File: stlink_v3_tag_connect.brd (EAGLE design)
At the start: 39.2 x 49.9 mm, 10 parts, among them CON1 STLINK_V3_HAT_SWD/JTAG_MINIMAL, J1 RJ12, U1 SN74LVC2T45DCU

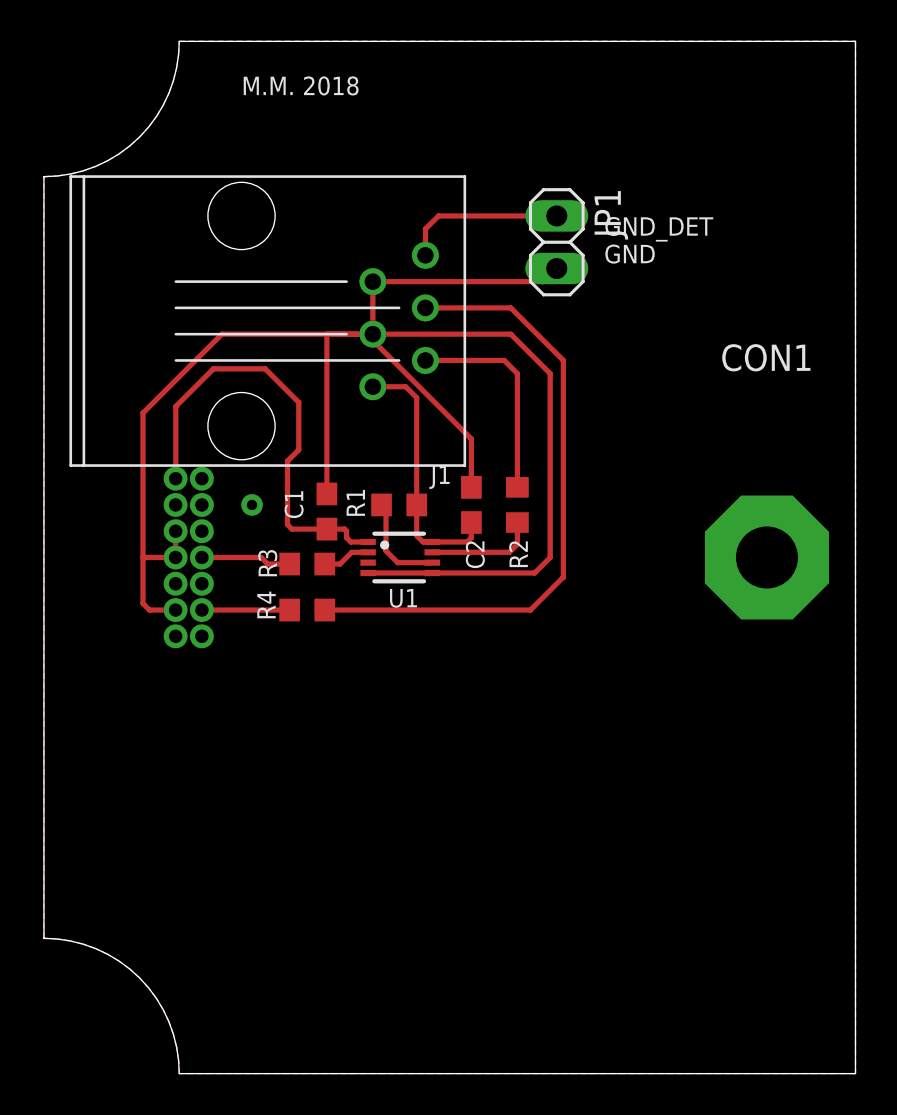
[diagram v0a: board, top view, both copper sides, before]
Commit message: Added SWD popoption
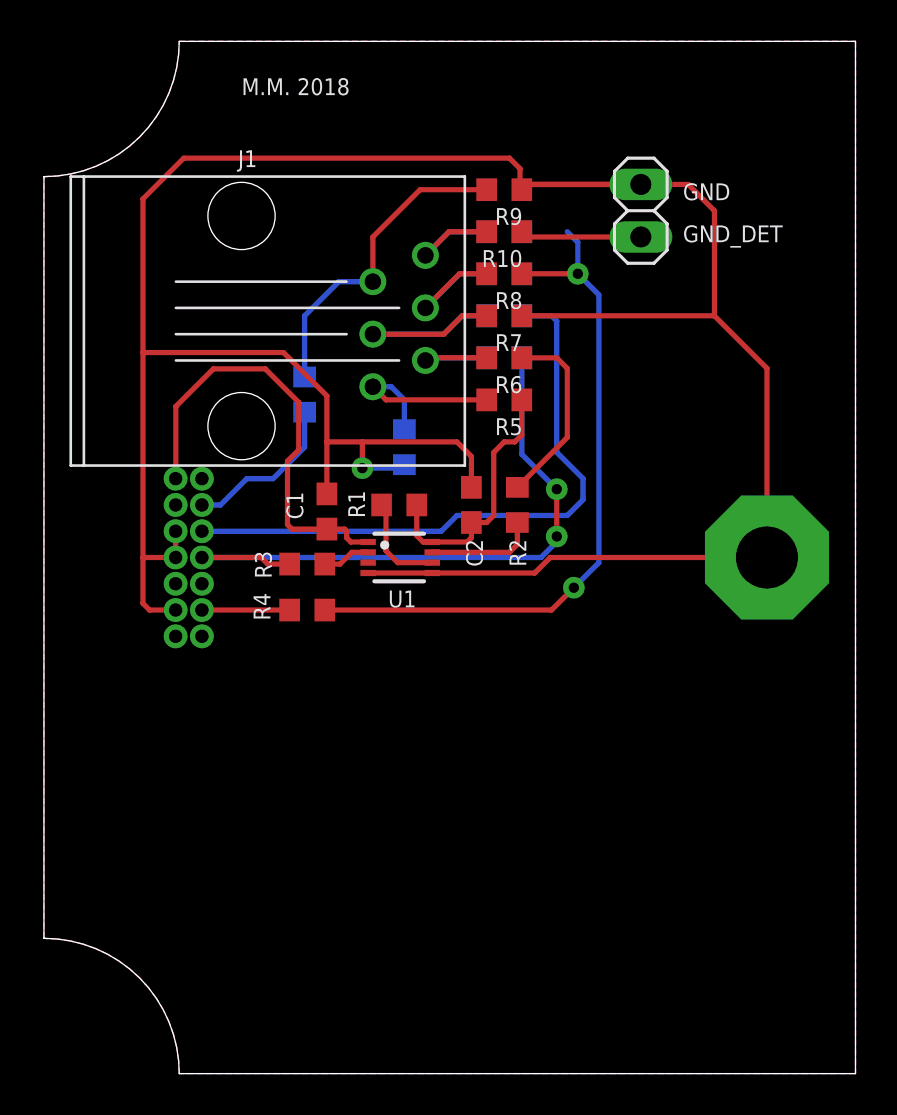
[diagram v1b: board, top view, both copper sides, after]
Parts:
- added R10, R11, R12, R13, R14, R15, R16, R5, R6, R7, R8, R9: 0, resistor:R0603
- JP1: value (none) -> -
- moved JP1 4.34 mm to (-6.10, 16.8), turned to 90 degrees
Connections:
- removed net SWIM_LVL_SHIFTED: CON1.STDC_14_8, R3.1
- removed net SWIM_TARGET: J1.5, R2.2
- removed net VCC_TARGET: C2.1, J1.6, R1.2, U1.8
- new net N$12: J1.6, R11.2, R5.2
- new net N$3: J1.5, R12.2, R6.2
- new net N$4: J1.4, R13.2, R7.2
- new net N$5: J1.3, R14.2, R8.2
- new net N$6: J1.2, R15.2, R9.2
- new net N$7: J1.1, R10.2, R16.2
- new net SWDCLK: CON1.STDC_14_6, R13.1
- new net SWDIO: CON1.STDC_14_4, R15.1
- new net SWIM_DATA: R2.2, R6.1
- new net SWO/SWIM_LVL_SHIFTED: CON1.STDC_14_8, R12.1, R3.1
- net !RESET_TARGET: now also R14.1, R8.1; no longer J1.3
- net DETECT: now also R10.1; no longer J1.1
- net GND: now also R11.1, R7.1, R9.1; no longer J1.2, J1.4
- net SWIM_TARGET_R: now also CON1.STDC_14_10
- net TARGET_VCC: now also C2.1, R1.2, R16.1, R5.1, U1.8
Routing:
- net GND: track 84.8 -> 133.3 mm
- net SWO/SWIM_LVL_SHIFTED: track 0.00 -> 31.4 mm, vias 0 -> 2
- net SWDCLK: track 0.00 -> 30.0 mm
- net N$6: track 0.00 -> 15.6 mm
- net TARGET_VCC: track 0.00 -> 12.7 mm
- net VCC_TARGET: track 12.6 -> 0.00 mm
- net N$4: track 0.00 -> 11.7 mm
- net SWIM_TARGET: track 10.2 -> 0.00 mm
- net SWIM_DATA: track 0.00 -> 9.16 mm
- net N$12: track 0.00 -> 8.99 mm
- net SWDIO: track 0.00 -> 7.81 mm
- net N$5: track 0.00 -> 7.29 mm
- net N$7: track 0.00 -> 6.87 mm
- net N$3: track 0.00 -> 6.03 mm
- net SWIM_LVL_SHIFTED: track 4.37 -> 0.00 mm
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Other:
- board text added: "GND GND_DET"
- board text removed: "GND_DET GND"

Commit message: Routing done
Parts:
- moved R16 7.15 mm to (-19.8, 15.0), turned to 180 degrees
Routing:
- net TARGET_VCC: track 12.7 -> 52.8 mm, vias 0 -> 1
- net SWIM_TARGET_R: track 5.33 -> 42.9 mm, vias 0 -> 2
- net !RESET_TARGET: track 33.5 -> 35.3 mm
- net SWDCLK: track 30.0 -> 31.5 mm
- net SWO/SWIM_LVL_SHIFTED: track 31.4 -> 32.7 mm
- net N$7: track 6.87 -> 6.04 mm
- net SWDIO: track 7.81 -> 8.41 mm

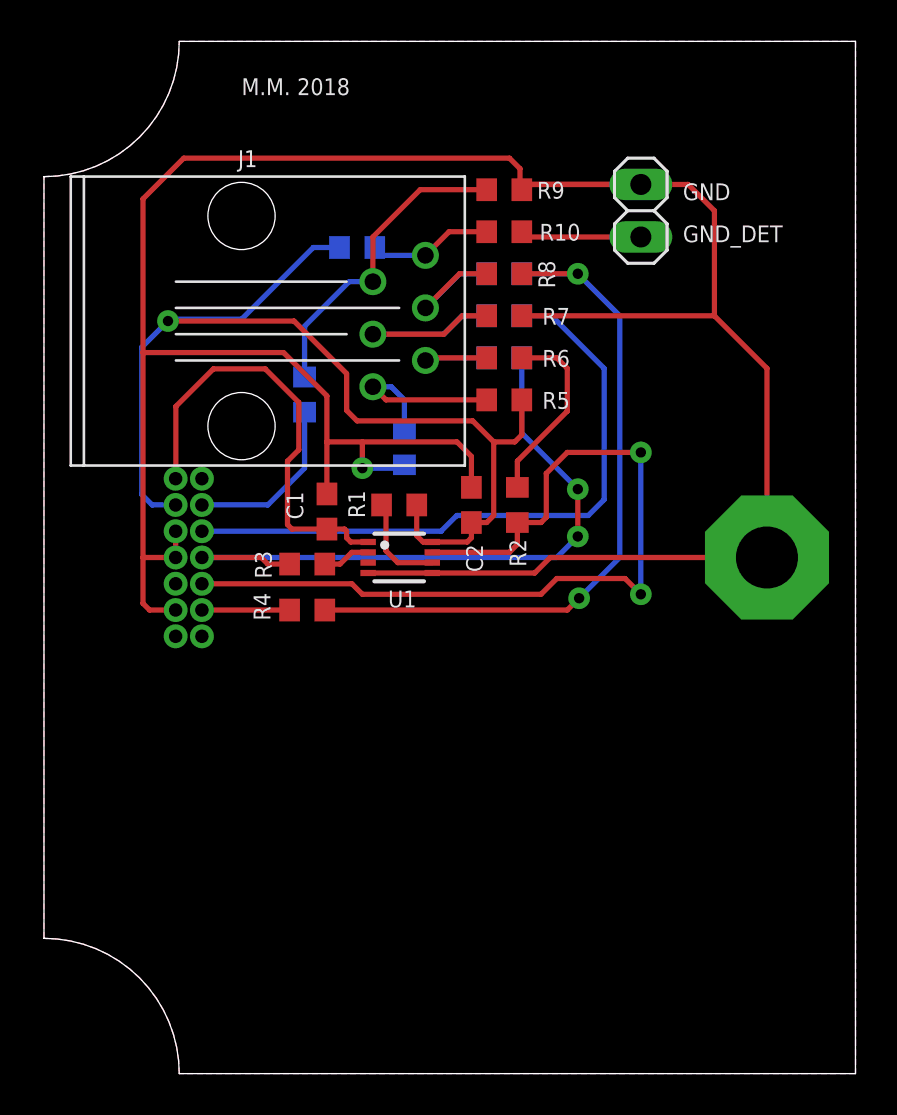
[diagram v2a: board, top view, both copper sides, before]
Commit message: - Added mgt MCU - Moved RJ12 to the middle - Fixed SWD pinout
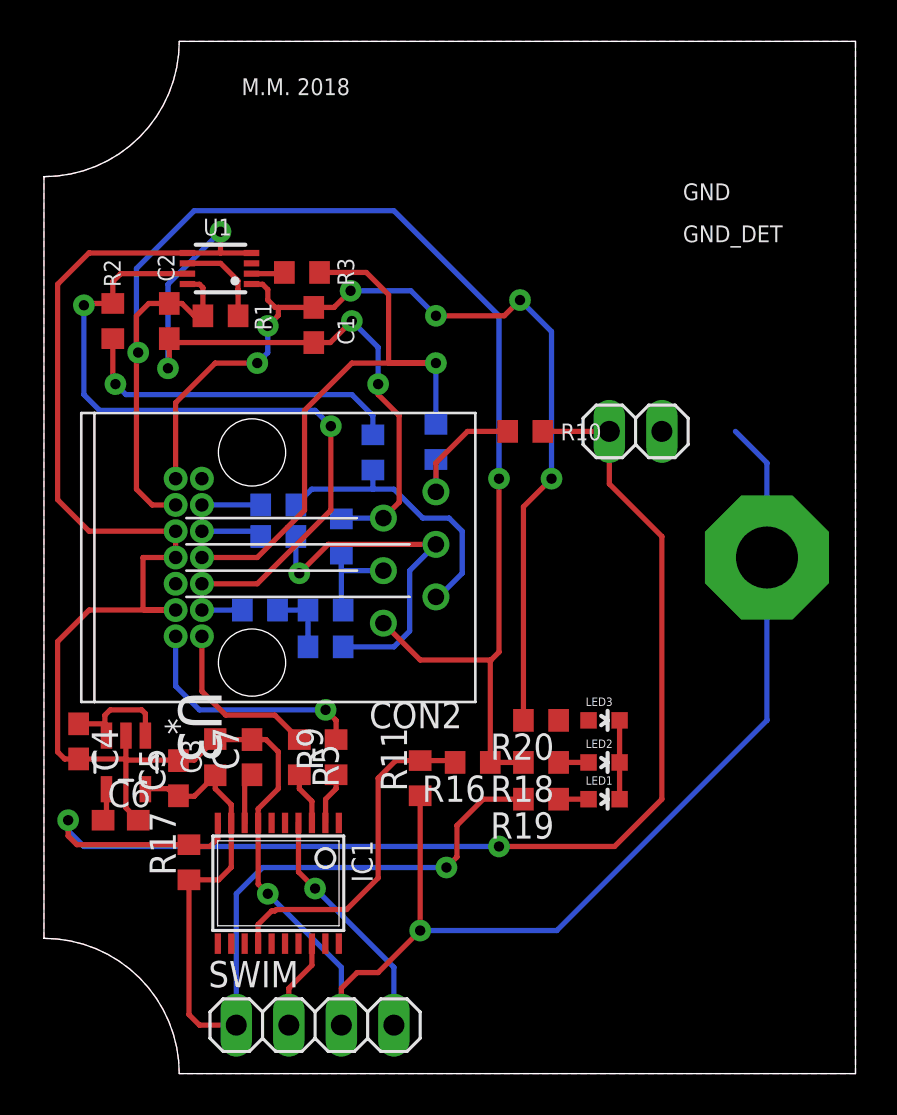
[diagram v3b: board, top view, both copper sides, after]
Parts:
- removed J1: RJ12, con-rj:RJ12
- added C3: 100nF, rcl:C0603K
- added C4, C5, C7: 1uF, rcl:C0603
- added C6: 470pF, rcl:C0603
- added CON2: TC2030-MCP-SWD, tag-connect:RJ12
- added IC1: STM8S003F3, stm8:TSSOP20
- added LED1, LED2, LED3: Red, SparkFun:LED-0603
- added R17: 10K, rcl:R0603
- added R18, R19, R20: 1K, rcl:R0603
- added SWIM: SWIM_254, swim:1X04
- added U3: MIC5205-3.3YM5-TR, LTC_By_element14_Batch_1:SOT95P280X145-5N
- R11, R16: value 0 -> 10K; device resistor:R0603 -> rcl:R0603
- R5, R9: value 0 -> 47; device resistor:R0603 -> rcl:R0603
- moved R9 28.6 mm to (-20.8, -9.65), turned to 90 degrees
- moved R16 25.5 mm to (-14.2, -9.91), flipped to the top
- moved R2 21.5 mm to (-31.6, 11.4), turned to 270 degrees
- moved R8 20.0 mm to (-21.3, -4.32), flipped to the bottom
- moved R5 19.9 mm to (-22.6, -9.65), turned to 270 degrees
- moved R14 18.4 mm to (-21.3, -2.54), turned to 180 degrees
- moved C2 17.1 mm to (-28.9, 11.4), turned to 270 degrees
- moved U1 16.4 mm to (-26.4, 14.0), turned to 90 degrees
- moved R11 16.0 mm to (-16.8, -10.7), flipped to the top
- moved R13 15.3 mm to (-23.6, 1.02), turned to 180 degrees
- moved R3 14.1 mm to (-22.5, 13.8), turned to 180 degrees
- moved R7 13.3 mm to (-20.6, 1.02), flipped to the bottom, turned to 270 degrees
- moved R1 12.6 mm to (-26.4, 11.7), turned to 180 degrees
- moved JP1 10.7 mm to (-6.35, 6.10), turned to 0 degrees
- moved R10 9.71 mm to (-11.7, 6.10)
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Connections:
- removed net N$12: J1.6, R11.2, R5.2
- removed net N$6: J1.2, R15.2, R9.2
- removed net N$7: J1.1, R10.2, R16.2
- new net !RESET_TARGET!/SWDCLK: CON2.3, R13.2, R8.2
- new net !RST: IC1.4, SWIM.4
- new net +3V3: C3.1, C5.1, IC1.9, R17.1, R19.2, SWIM.1, U3.5
- new net DETECT/SWO: CON2.1, R10.2, R12.2
- new net DGND: LED1.C, LED2.C, LED3.C
- new net GND/!RESET_TARGET!: CON2.4, R14.2, R7.2
- new net MIC_BYPASS: C6.1, U3.4
- new net N$2: CON1.STDC_14_14, R5.1
- new net N$38: LED2.A, R18.1
- new net STM8_RX: IC1.3, R5.2
- new net STM8_SWIM: IC1.18, SWIM.2
- new net STM8_TX: IC1.2, R9.1
- new net SWIM_DATA/SWDIO: CON2.5, R15.2, R6.2
- new net TARGET_VCC_DETECT: IC1.14, R11.2, R16.2
- new net VBAT: C4.1, U3.1, U3.3
- new net VCAP1: C7.1, IC1.8
- net DETECT: now also IC1.10, R17.2
- net GND: now also C3.2, C4.2, C5.2, C6.2, C7.2, CON2.2, IC1.7, SWIM.3, U3.2; no longer R9.1
- net N$3: now also CON1.STDC_14_13, R9.2; no longer J1.5, R12.2, R6.2
- net N$4: now also LED1.A, R19.1; no longer J1.4, R13.2, R7.2
- net N$5: now also LED3.A, R20.1; no longer J1.3, R14.2, R8.2
- net TARGET_VCC: now also CON2.6, R18.2; no longer R5.1
- net VUSB: now also R20.2
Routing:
- net DETECT: track 5.86 -> 61.6 mm, vias 0 -> 2
- net +3V3: track 0.00 -> 43.2 mm, vias 0 -> 1
- net !RESET_TARGET: track 35.3 -> 3.25 mm, vias 2 -> 0
- net SWDCLK: track 31.5 -> 3.10 mm
- net VUSB: track 21.4 -> 47.9 mm, vias 0 -> 6
- net GND: track 133.3 -> 157.6 mm, vias 1 -> 6
- net TARGET_VCC: track 52.8 -> 71.1 mm, vias 1 -> 2
- net !RESET_TARGET!/SWDCLK: track 0.00 -> 17.3 mm, vias 0 -> 1
- net TARGET_VCC_DETECT: track 0.00 -> 16.6 mm
- net N$6: track 15.3 -> 0.00 mm
- net SWIM_DATA/SWDIO: track 0.00 -> 13.9 mm
- net !RST: track 0.00 -> 11.7 mm, vias 0 -> 1
- net N$4: track 11.7 -> 1.45 mm
- net N$12: track 8.99 -> 0.00 mm
- net N$2: track 0.00 -> 8.33 mm
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
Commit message: Align LEDs
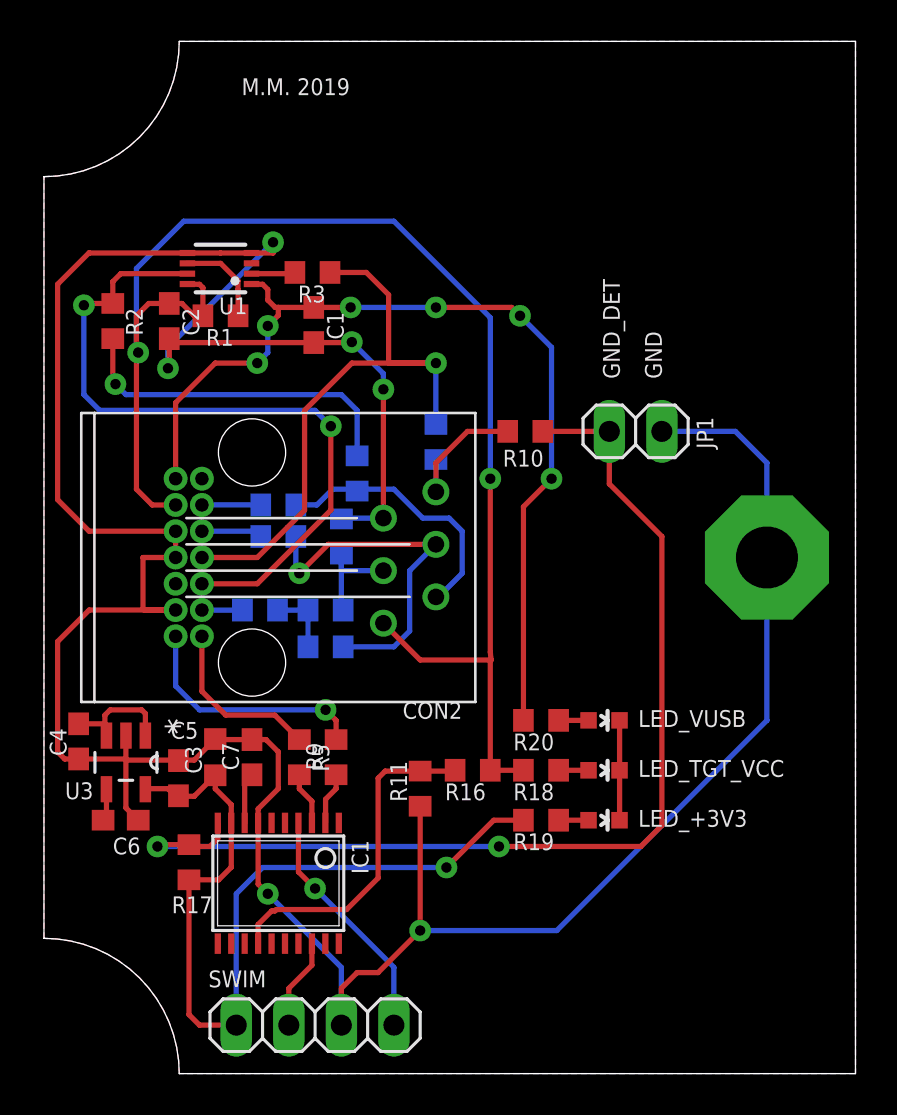
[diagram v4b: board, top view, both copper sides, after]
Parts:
- removed LED1, LED2: Red, SparkFun:LED-0603
- added LED_+3V3, LED_TGT_VCC: Red, SparkFun:LED-0603
- moved R6 1.27 mm to (-19.8, 4.06)
- moved R19 1.02 mm to (-10.9, -12.7)
- moved R11 0.51 mm to (-16.8, -11.2)
- moved R3 0.51 mm to (-22.0, 13.8)
- moved R16 0.38 mm to (-14.2, -10.3)
- moved R18 0.38 mm to (-10.9, -10.3)
- renumbered LED3 to LED_VUSB
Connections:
- net DGND: now also LED_+3V3.C, LED_TGT_VCC.C; no longer LED1.C, LED2.C
- net N$38: now also LED_TGT_VCC.A; no longer LED2.A
- net N$4: now also LED_+3V3.A; no longer LED1.A
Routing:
- net DETECT: track 61.6 -> 52.0 mm
- net GND: track 157.6 -> 159.6 mm
- net VUSB: track 47.9 -> 46.2 mm
- net N$5: track 0.00 -> 1.45 mm
- net +3V3: track 43.2 -> 41.9 mm
- net DGND: track 3.81 -> 4.83 mm
- net SWIM_DATA/SWDIO: track 13.9 -> 13.1 mm
- net TARGET_VCC: track 71.1 -> 70.4 mm
- net SWO/SWIM_LVL_SHIFTED: track 30.4 -> 29.9 mm
- net SWIM_LVL_SHIFTED_R: track 1.61 -> 2.12 mm
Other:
- board text added: "GND_DET GND"
- board text added: "M.M. 2019"
- board text removed: "GND GND_DET"
- board text removed: "M.M. 2018"
